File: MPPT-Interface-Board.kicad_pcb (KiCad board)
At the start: 2 copper layers, 41.8 x 42.8 mm, 39 parts, among them J1 MPPT A, J2 MPPT X, J3 CarCAN In, J4 CarCAN Out, J5 FUSEBOX, Q1 PMV35EPER, U1 RI3-1209S

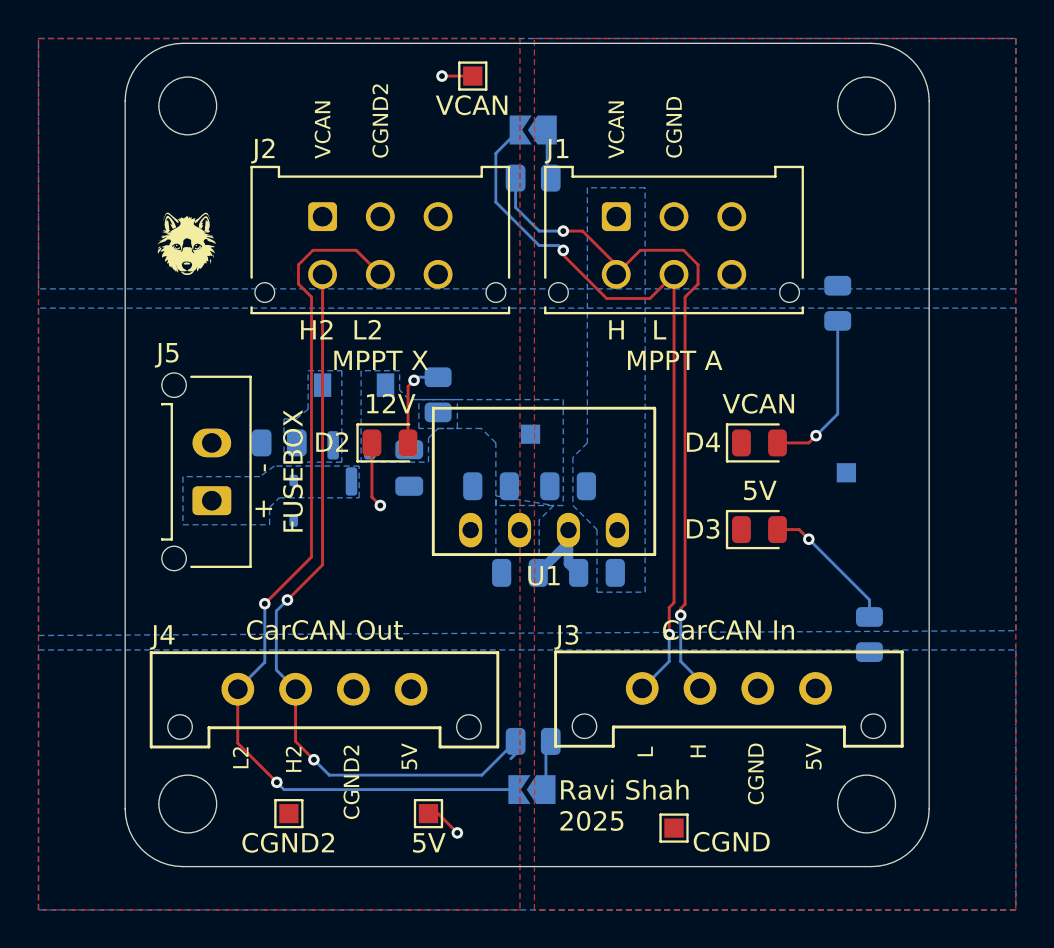
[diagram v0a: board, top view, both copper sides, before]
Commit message: make gndpwr larger
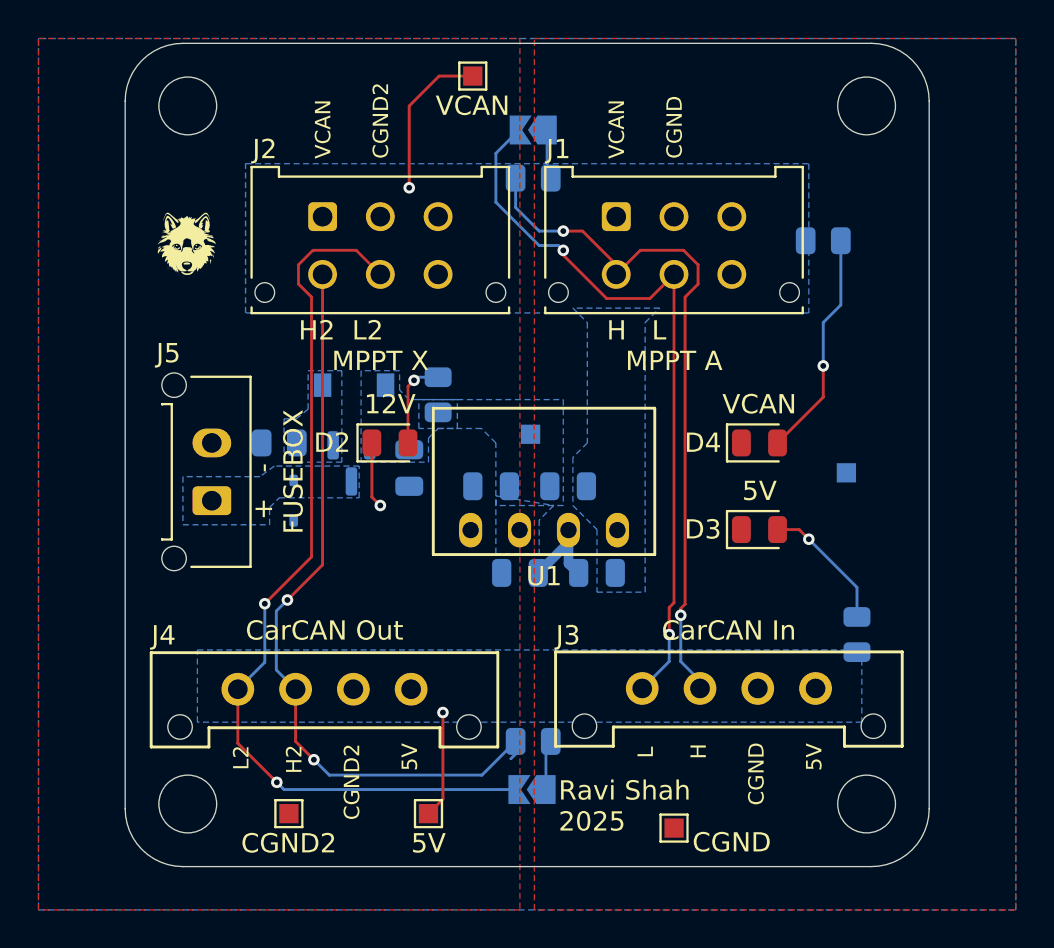
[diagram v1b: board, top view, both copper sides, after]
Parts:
- moved R5 3.34 mm to (132.0, 72.8), turned to 0 degrees
- moved R4 0.65 mm to (133.8, 93.2)
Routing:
- net V_CAN: track 1.60 -> 8.19 mm
- net +5V: track 1.91 -> 5.56 mm
- net Net-(D4-A): track 8.58 -> 11.9 mm

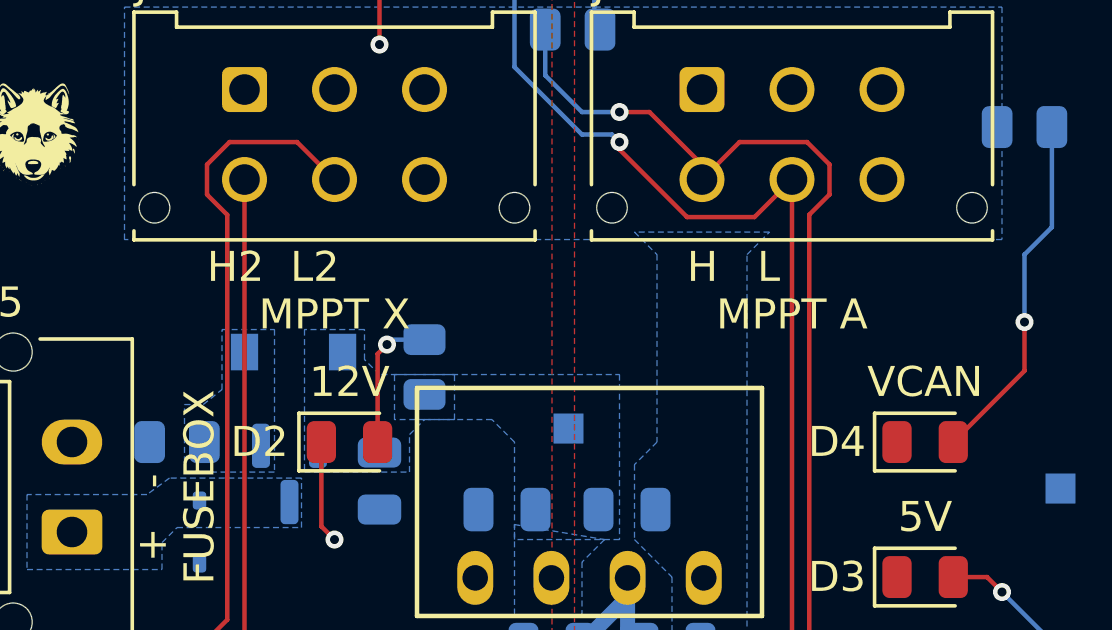
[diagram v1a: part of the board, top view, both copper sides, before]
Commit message: lakshay make board black pls
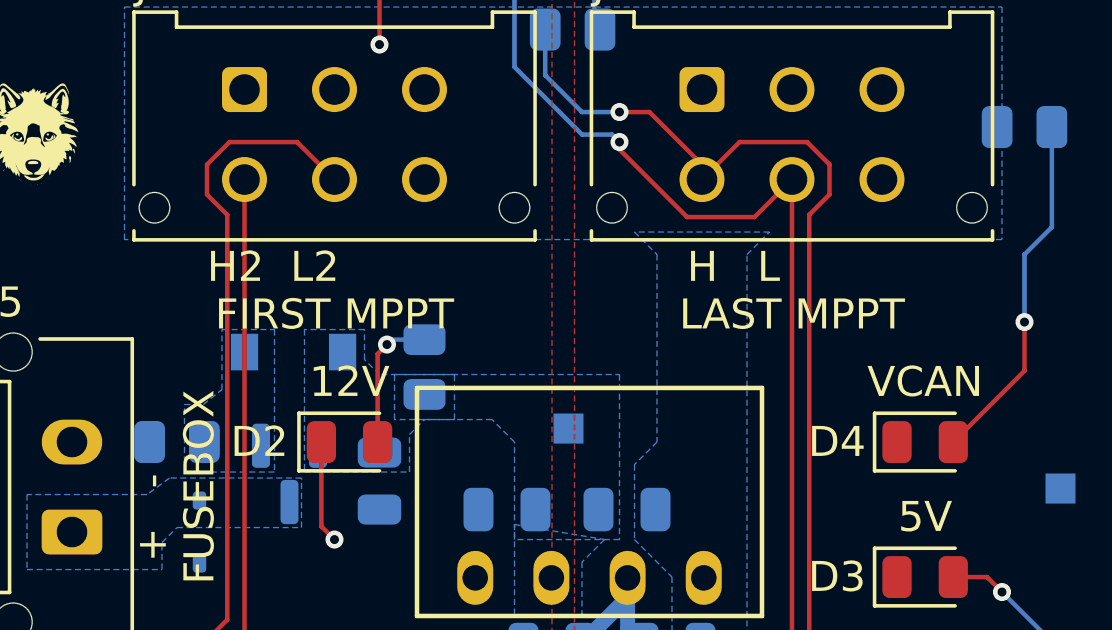
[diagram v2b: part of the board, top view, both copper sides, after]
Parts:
- J1: value MPPT A -> LAST MPPT
- J2: value MPPT X -> FIRST MPPT
- moved LOGO1 0.54 mm to (127.0, 84.8)

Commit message: wow
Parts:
- J1: value LAST MPPT -> FIRST MPPT
- J2: value FIRST MPPT -> LAST MPPT
- moved LOGO1 0.25 mm to (127.0, 85.0)
